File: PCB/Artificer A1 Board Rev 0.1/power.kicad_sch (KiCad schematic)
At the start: 78 parts, among them U10 AXP717B, U11 AXP323, U9 SY8089A1AAC

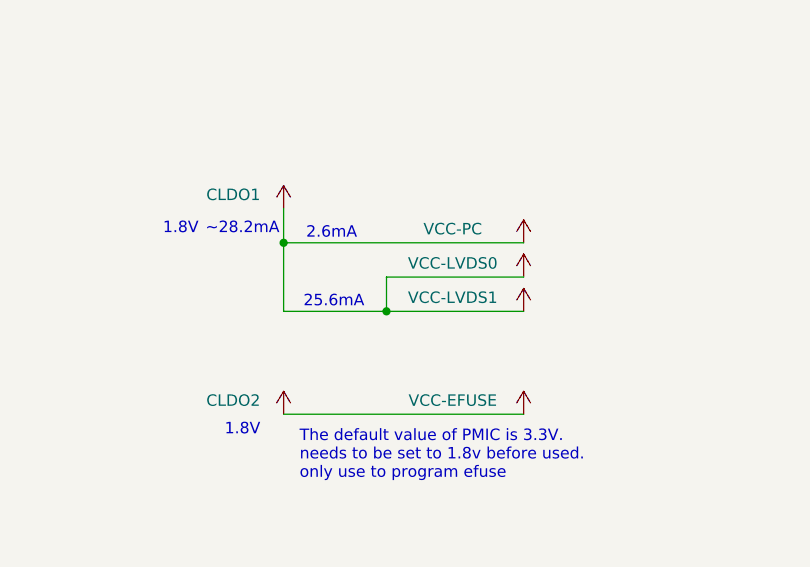
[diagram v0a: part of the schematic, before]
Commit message: added power and gnd vias
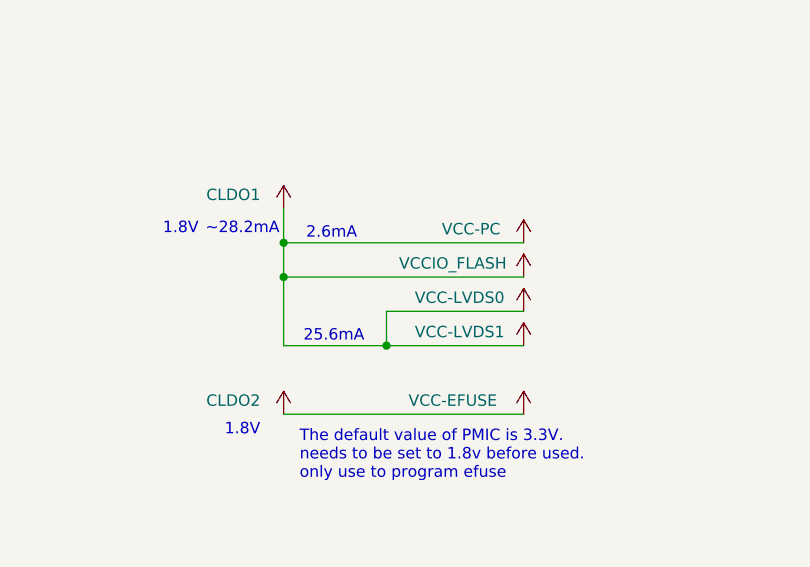
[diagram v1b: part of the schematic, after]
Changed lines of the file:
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@@
 	(text "25.6mA"
 		(exclude_from_sim no)
-		(at 168.148 166.624 0)
+		(at 168.148 170.434 0)
 		(effects
 			(font
@@
 	)
 	(junction
+		(at 162.56 163.83)
+		(diameter 0)
+		(color 0 0 0 0)
+	)
+	(junction
 		(at 209.55 119.38)
 		(diameter 0)
@@
 	)
 	(junction
-		(at 173.99 167.64)
+		(at 173.99 171.45)
 		(diameter 0)
 		(color 0 0 0 0)
@@
 	(wire
 		(pts
+			(xy 162.56 163.83) (xy 162.56 171.45)
+		)
+		(stroke
+			(width 0)
+			(type default)
+		)
+	)
+	(wire
+		(pts
 			(xy 218.44 36.83) (xy 245.11 36.83)
 		)
@@
 	(wire
 		(pts
+			(xy 162.56 163.83) (xy 189.23 163.83)
+		)
+		(stroke
+			(width 0)
+			(type default)
+		)
+	)
+	(wire
+		(pts
 			(xy 30.48 200.66) (xy 30.48 196.85)
 		)
@@
 	(wire
 		(pts
-			(xy 173.99 167.64) (xy 162.56 167.64)
+			(xy 173.99 171.45) (xy 162.56 171.45)
 		)
 		(stroke
@@
 	(wire
 		(pts
-			(xy 173.99 163.83) (xy 173.99 167.64)
+			(xy 173.99 167.64) (xy 173.99 171.45)
 		)
 		(stroke
@@
 	(wire
 		(pts
-			(xy 173.99 167.64) (xy 189.23 167.64)
+			(xy 173.99 171.45) (xy 189.23 171.45)
 		)
 		(stroke
@@
 	(wire
 		(pts
-			(xy 162.56 160.02) (xy 162.56 167.64)
+			(xy 162.56 160.02) (xy 162.56 163.83)
 		)
 		(stroke
@@
 	(wire
 		(pts
-			(xy 173.99 163.83) (xy 189.23 163.83)
+			(xy 173.99 167.64) (xy 189.23 167.64)
 		)
 		(stroke
@@
 	(symbol
 		(lib_id "power:+5V")
-		(at 189.23 163.83 0)
+		(at 189.23 167.64 0)
 		(unit 1)
 		(body_style 1)
@@
 		(dnp no)
 		(property "Reference" "#PWR0152"
-			(at 189.23 167.64 0)
+			(at 189.23 171.45 0)
 			(hide yes)
 			(show_name no)
@@
 		)
 		(property "Value" "VCC-LVDS0"
-			(at 181.356 162.306 0)
+			(at 182.118 166.116 0)
 			(show_name no)
 			(do_not_autoplace no)
@@
 		)
 		(property "Footprint" ""
-			(at 189.23 163.83 0)
+			(at 189.23 167.64 0)
 			(hide yes)
 			(show_name no)
@@
 		)
 		(property "Datasheet" ""
-			(at 189.23 163.83 0)
+			(at 189.23 167.64 0)
 			(hide yes)
 			(show_name no)
@@
 		)
 		(property "Description" "Power symbol creates a global label with name \"+5V\""
-			(at 189.23 163.83 0)
+			(at 189.23 167.64 0)
 			(hide yes)
 			(show_name no)
@@
 		)
 		(property "Value" "VCC-PC"
-			(at 181.356 158.496 0)
+			(at 183.388 158.496 0)
 			(show_name no)
 			(do_not_autoplace no)
@@
 	)
 	(symbol
+		(lib_id "power:VDD")
+		(at 189.23 163.83 0)
+		(unit 1)
+		(body_style 1)
+		(exclude_from_sim no)
+		(in_bom yes)
+		(on_board yes)
+		(in_pos_files yes)
+		(dnp no)
+		(property "Reference" "#PWR081"
+			(at 189.23 167.64 0)
+			(hide yes)
+			(show_name no)
+			(do_not_autoplace no)
+			(effects
+				(font
+					(size 1.27 1.27)
+				)
+			)
+		)
+		(property "Value" "VCCIO_FLASH"
+			(at 181.356 162.306 0)
+			(show_name no)
+			(do_not_autoplace no)
+			(effects
+				(font
+					(size 1.27 1.27)
+				)
+			)
+		)
+		(property "Footprint" ""
+			(at 189.23 163.83 0)
+			(hide yes)
+			(show_name no)
+			(do_not_autoplace no)
+			(effects
+				(font
+					(size 1.27 1.27)
+				)
+			)
+		)
+		(property "Datasheet" ""
+			(at 189.23 163.83 0)
+			(hide yes)
+			(show_name no)
+			(do_not_autoplace no)
+			(effects
+				(font
+					(size 1.27 1.27)
+				)
+			)
+		)
+		(property "Description" "Power symbol creates a global label with name \"VDD\""
+			(at 189.23 163.83 0)
+			(hide yes)
+			(show_name no)
+			(do_not_autoplace no)
+			(effects
+				(font
+					(size 1.27 1.27)
+				)
+			)
+		)
+		(pin "1"
+		)
+		(instances
+			(project "Artificer A1 Board Rev 0.1"
+				(path "/7c37bdb5-94b0-4567-b5ec-a879db855389/ae3e07ef-f034-4788-a69a-5dbad0c7ebc1"
+					(reference "#PWR081")
+					(unit 1)
+				)
+			)
+		)
+	)
+	(symbol
 		(lib_id "Cap:JLCPCB_Lib_Blank_Cap")
 		(at 240.03 133.35 180)
@@
 	(symbol
 		(lib_id "power:+5V")
-		(at 189.23 167.64 0)
+		(at 189.23 171.45 0)
 		(unit 1)
 		(body_style 1)
@@
 		(dnp no)
 		(property "Reference" "#PWR0153"
-			(at 189.23 171.45 0)
+			(at 189.23 175.26 0)
 			(hide yes)
 			(show_name no)
@@
 		)
 		(property "Value" "VCC-LVDS1"
-			(at 181.356 166.116 0)
+			(at 182.118 169.926 0)
 			(show_name no)
 			(do_not_autoplace no)
@@
 		)
 		(property "Footprint" ""
-			(at 189.23 167.64 0)
+			(at 189.23 171.45 0)
 			(hide yes)
 			(show_name no)
@@
 		)
 		(property "Datasheet" ""
-			(at 189.23 167.64 0)
+			(at 189.23 171.45 0)
 			(hide yes)
 			(show_name no)
@@
 		)
 		(property "Description" "Power symbol creates a global label with name \"+5V\""
-			(at 189.23 167.64 0)
+			(at 189.23 171.45 0)
 			(hide yes)
 			(show_name no)

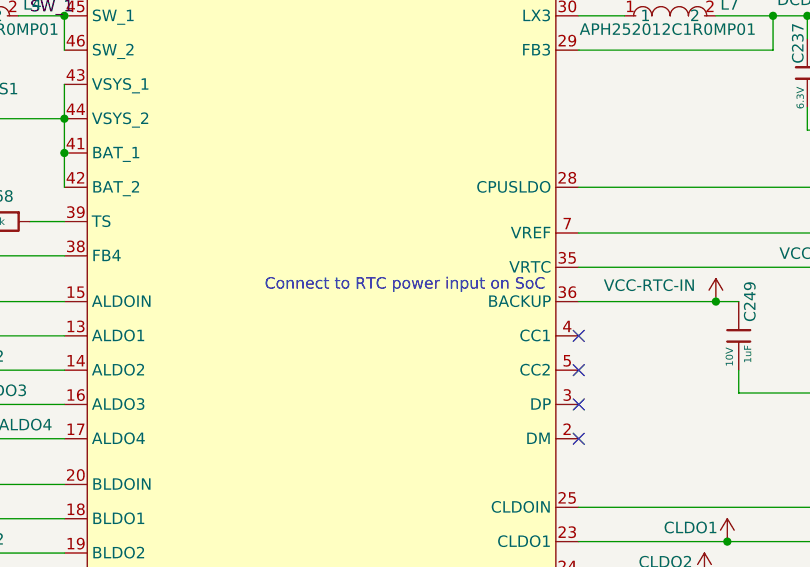
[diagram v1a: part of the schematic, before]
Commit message: added fan and PD debugging circuitry
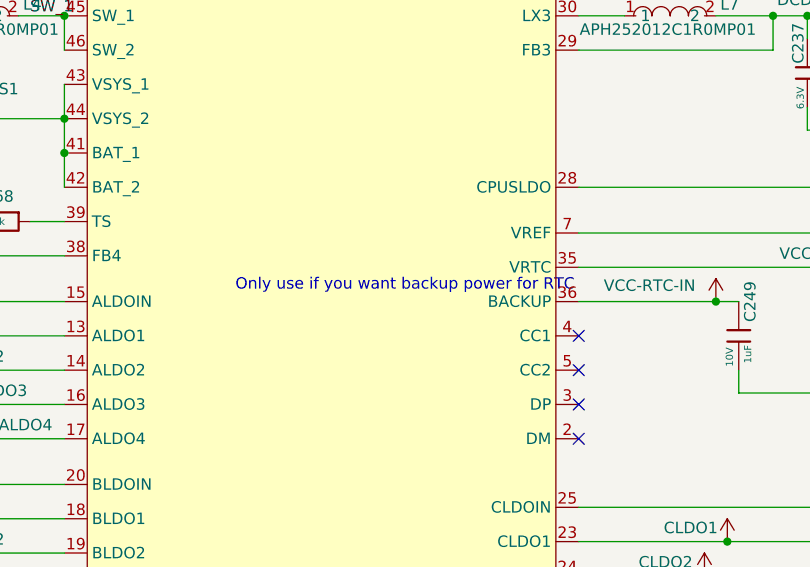
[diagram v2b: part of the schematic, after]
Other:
- note added: "Only use if you want backup power for RTC"
- note removed: "Connect to RTC power input on SoC"
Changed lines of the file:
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@@
 		)
 	)
-	(text "Connect to RTC power input on SoC"
+	(text "Only use if you want backup power for RTC"
 		(exclude_from_sim no)
 		(at 299.466 92.202 0)
